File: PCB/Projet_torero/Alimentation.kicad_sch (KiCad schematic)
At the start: 17 parts, among them IC501 MP1475SGJ-P, J501 Conn_01x02, SW501 SW_DPDT_x2, U501 BU33SD5WG-TR

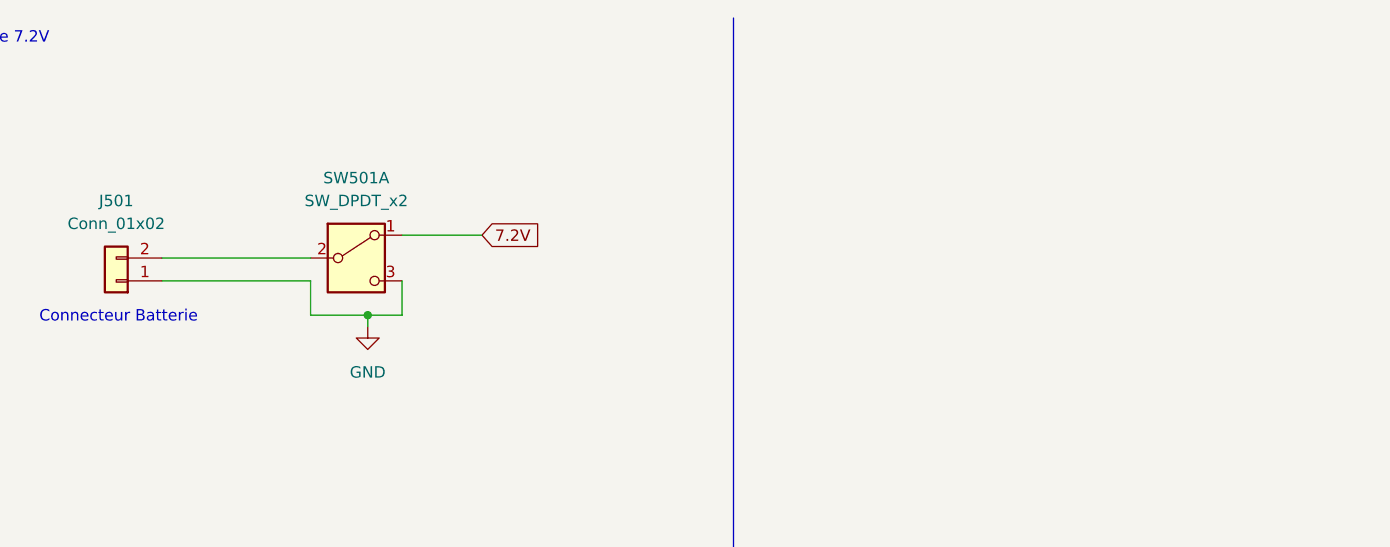
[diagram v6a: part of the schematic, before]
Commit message: Refait l'alimentation
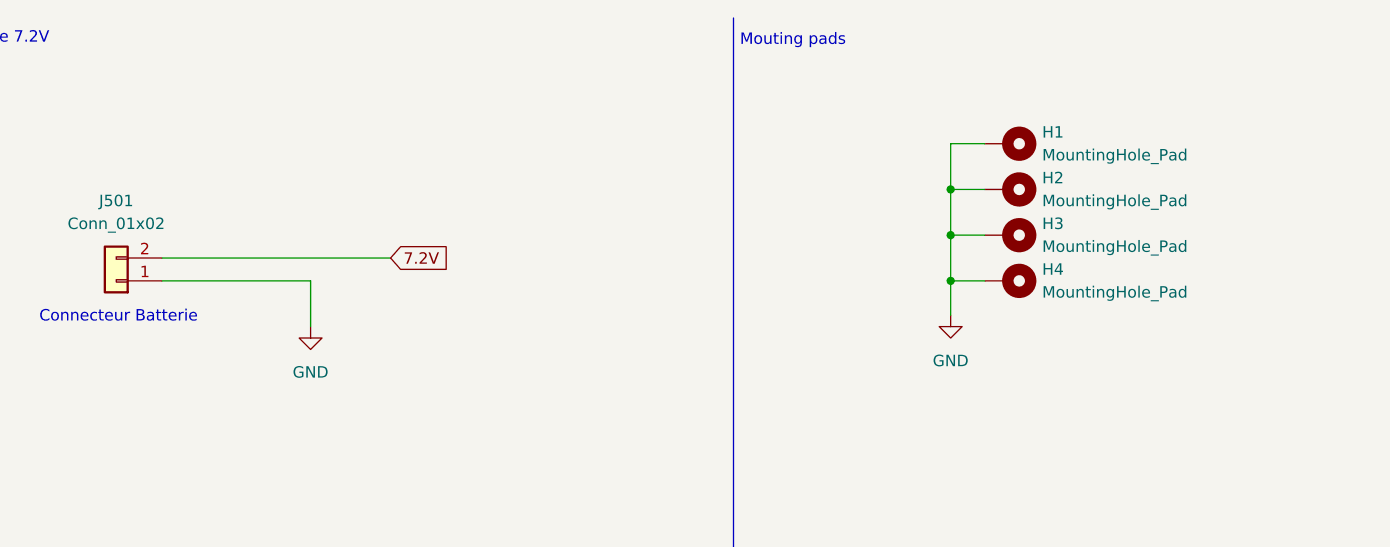
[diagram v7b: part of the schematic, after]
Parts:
- removed SW501: SW_DPDT_x2, symbol Switch:SW_DPDT_x2
- added H1, H2, H3, H4: MountingHole_Pad, MountingHole:MountingHole_3.2mm_M3_Pad_Via, symbol Mechanical:MountingHole_Pad
- IC501: footprint SOT65P280X100-8N -> Mp:SOT65P280X100-8N
- U501: footprint SSOP5_ROM -> BU33:SOT95P280X125-5N
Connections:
- net 7.2V: now also J501.2 (Pin_2)
- net GND: now also H1.1, H2.1, H3.1, H4.1
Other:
- note added: "Mouting pads"

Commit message: Mis à jour des composants
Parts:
- added J202: Conn_02x02_Odd_Even, symbol Connector_Generic:Conn_02x02_Odd_Even
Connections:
- net 7.2V: now also J202.2 (Pin_2); no longer J501.2 (Pin_2)
- net GND: now also J202.4 (Pin_4)
- new net: J202.1 (Pin_1), J501.2 (Pin_2)
- no-connect marks 0 -> 1
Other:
- note added: "Connecteur Switch ON/OFF"
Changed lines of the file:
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@@
 		(color 0 0 0 0)
 	)
+	(junction
+		(at 57.15 44.45)
+		(diameter 0)
+		(color 0 0 0 0)
+	)
+	(no_connect
+		(at 46.99 40.64)
+	)
 	(polyline
 		(pts
@@
 	(wire
 		(pts
+			(xy 63.5 40.64) (xy 63.5 44.45)
+		)
+		(stroke
+			(width 0)
+			(type default)
+		)
+	)
+	(wire
+		(pts
 			(xy 203.2 120.65) (xy 203.2 127)
 		)
@@
 	(wire
 		(pts
+			(xy 63.5 44.45) (xy 57.15 44.45)
+		)
+		(stroke
+			(width 0)
+			(type default)
+		)
+	)
+	(wire
+		(pts
 			(xy 227.33 138.43) (xy 227.33 139.7)
 		)
@@
 	(wire
 		(pts
+			(xy 44.45 40.64) (xy 44.45 44.45)
+		)
+		(stroke
+			(width 0)
+			(type default)
+		)
+	)
+	(wire
+		(pts
 			(xy 71.12 152.4) (xy 64.77 152.4)
 		)
@@
 	(wire
 		(pts
-			(xy 57.15 40.64) (xy 57.15 45.72)
-		)
-		(stroke
-			(width 0)
-			(type default)
-		)
-	)
-	(wire
-		(pts
-			(xy 57.15 40.64) (xy 40.64 40.64)
-		)
-		(stroke
-			(width 0)
-			(type default)
-		)
-	)
-	(wire
-		(pts
 			(xy 127 156.21) (xy 127 161.29)
 		)
@@
 	(wire
 		(pts
+			(xy 59.69 40.64) (xy 63.5 40.64)
+		)
+		(stroke
+			(width 0)
+			(type default)
+		)
+	)
+	(wire
+		(pts
+			(xy 59.69 38.1) (xy 66.04 38.1)
+		)
+		(stroke
+			(width 0)
+			(type default)
+		)
+	)
+	(wire
+		(pts
 			(xy 115.57 153.67) (xy 115.57 156.21)
 		)
@@
 	(wire
 		(pts
+			(xy 40.64 38.1) (xy 46.99 38.1)
+		)
+		(stroke
+			(width 0)
+			(type default)
+		)
+	)
+	(wire
+		(pts
 			(xy 62.23 138.43) (xy 71.12 138.43)
 		)
@@
 	(wire
 		(pts
-			(xy 40.64 38.1) (xy 66.04 38.1)
-		)
-		(stroke
-			(width 0)
-			(type default)
-		)
-	)
-	(wire
-		(pts
 			(xy 128.27 35.56) (xy 128.27 30.48)
 		)
@@
 	(wire
 		(pts
+			(xy 44.45 44.45) (xy 57.15 44.45)
+		)
+		(stroke
+			(width 0)
+			(type default)
+		)
+	)
+	(wire
+		(pts
 			(xy 71.12 147.32) (xy 71.12 152.4)
+		)
+		(stroke
+			(width 0)
+			(type default)
+		)
+	)
+	(wire
+		(pts
+			(xy 44.45 40.64) (xy 40.64 40.64)
+		)
+		(stroke
+			(width 0)
+			(type default)
+		)
+	)
+	(wire
+		(pts
+			(xy 57.15 44.45) (xy 57.15 49.53)
 		)
 		(stroke
@@
 		)
 	)
+	(text "Connecteur Switch ON/OFF"
+		(exclude_from_sim no)
+		(at 54.61 28.194 0)
+		(effects
+			(font
+				(size 1.27 1.27)
+			)
+		)
+	)
 	(text "Régulateur tension 5V"
 		(exclude_from_sim no)
@@
 	(text "Connecteur Batterie"
 		(exclude_from_sim no)
-		(at 35.814 44.704 0)
+		(at 31.242 44.704 0)
 		(effects
 			(font
@@
 	)
 	(symbol
+		(lib_id "Connector_Generic:Conn_02x02_Odd_Even")
+		(at 52.07 38.1 0)
+		(unit 1)
+		(exclude_from_sim no)
+		(in_bom yes)
+		(on_board yes)
+		(dnp no)
+		(fields_autoplaced yes)
+		(property "Reference" "J202"
+			(at 53.34 31.75 0)
+			(effects
+				(font
+					(size 1.27 1.27)
+				)
+			)
+		)
+		(property "Value" "Conn_02x02_Odd_Even"
+			(at 53.34 34.29 0)
+			(effects
+				(font
+					(size 1.27 1.27)
+				)
+			)
+		)
+		(property "Footprint" ""
+			(at 52.07 38.1 0)
+			(effects
+				(font
+					(size 1.27 1.27)
+				)
+				(hide yes)
+			)
+		)
+		(property "Datasheet" "~"
+			(at 52.07 38.1 0)
+			(effects
+				(font
+					(size 1.27 1.27)
+				)
+				(hide yes)
+			)
+		)
+		(property "Description" "Generic connector, double row, 02x02, odd/even pin numbering scheme (row 1 odd numbers, row 2 even numbers), script generated (kicad-library-utils/schlib/autogen/connector/)"
+			(at 52.07 38.1 0)
+			(effects
+				(font
+					(size 1.27 1.27)
+				)
+				(hide yes)
+			)
+		)
+		(pin "3"
+		)
+		(pin "4"
+		)
+		(pin "2"
+		)
+		(pin "1"
+		)
+		(instances
+			(project ""
+				(path "/04e1eb47-a2c4-462b-bef7-377d9515a2c0/b3b2826c-2e3c-42fe-bcd6-22fcd6249c25"
+					(reference "J202")
+					(unit 1)
+				)
+			)
+		)
+	)
+	(symbol
 		(lib_id "power:GND")
-		(at 57.15 45.72 0)
+		(at 57.15 49.53 0)
 		(unit 1)
 		(exclude_from_sim no)
@@
 		(fields_autoplaced yes)
 		(property "Reference" "#PWR0503"
-			(at 57.15 52.07 0)
+			(at 57.15 55.88 0)
 			(effects
 				(font
@@
 		)
 		(property "Value" "GND"
-			(at 57.15 50.8 0)
+			(at 57.15 54.61 0)
 			(effects
 				(font
@@
 		)
 		(property "Footprint" ""
-			(at 57.15 45.72 0)
+			(at 57.15 49.53 0)
 			(effects
 				(font
@@
 		)
 		(property "Datasheet" ""
-			(at 57.15 45.72 0)
+			(at 57.15 49.53 0)
 			(effects
 				(font
@@
 		)
 		(property "Description" "Power symbol creates a global label with name \"GND\" , ground"
-			(at 57.15 45.72 0)
-			(effects
-				(font
+			(at 57.15 49.53 0)
+			(effects
+				(font
